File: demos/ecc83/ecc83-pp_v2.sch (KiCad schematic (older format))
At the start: 11 parts, among them P1 IN, P2 OUT, P3 POWER, P4 CONN_2, U1 ECC83

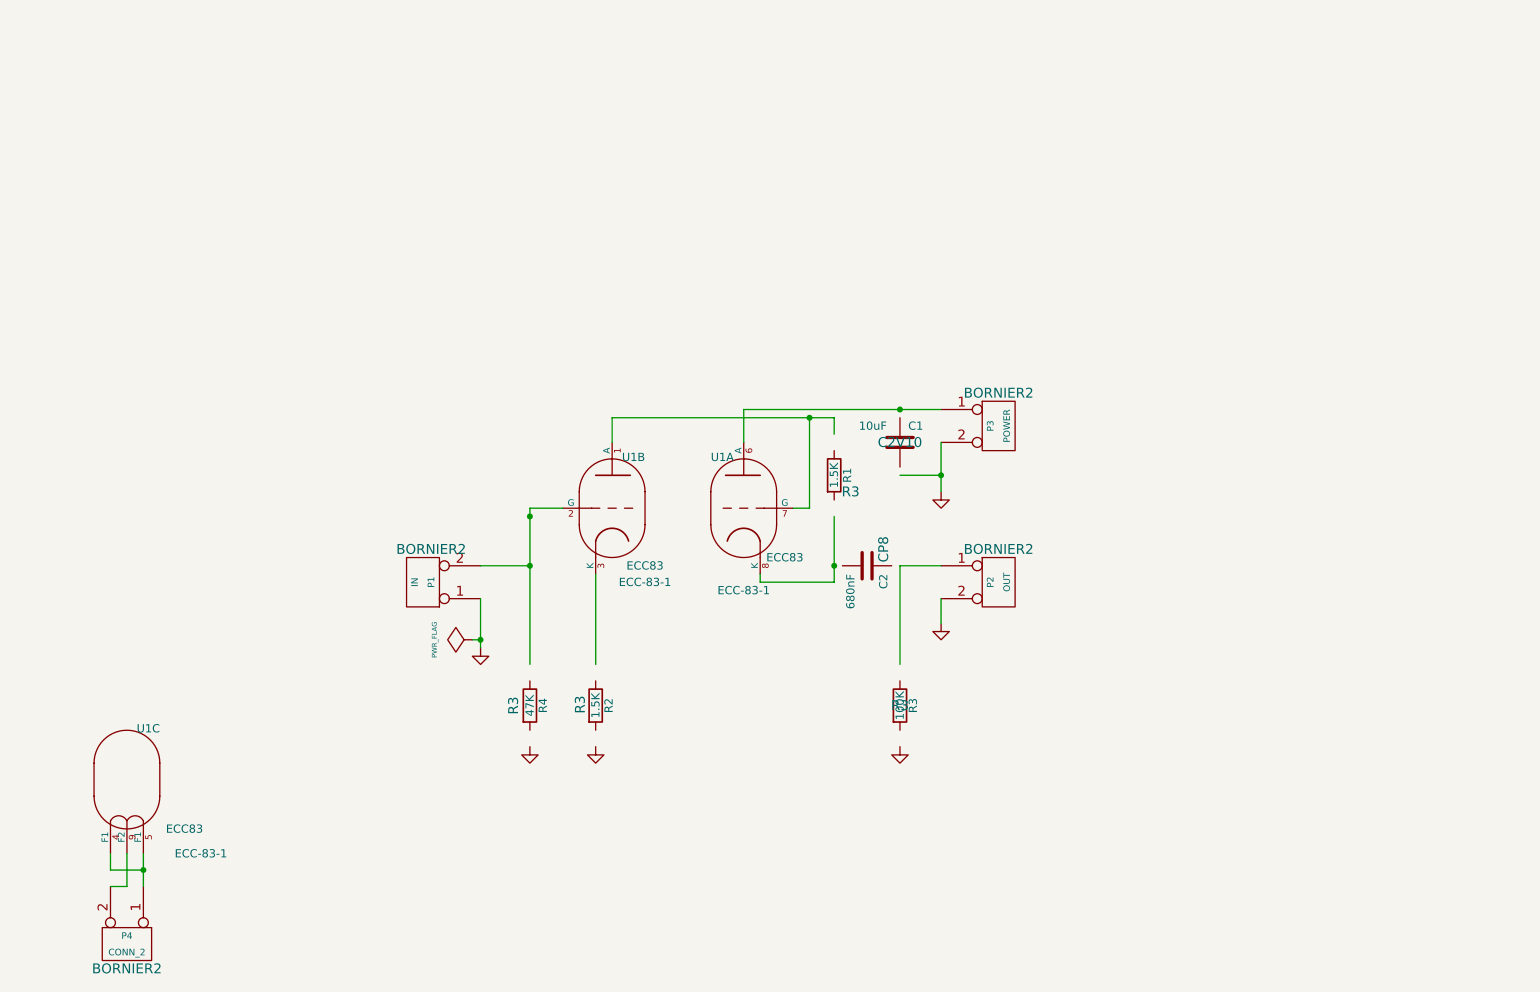
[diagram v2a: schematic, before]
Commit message: Update ecc83 demo. default KISYS3DMOD definition on Linux: add /usr/local/kicad/share/kicad/module/package3d test to find a suitable value.
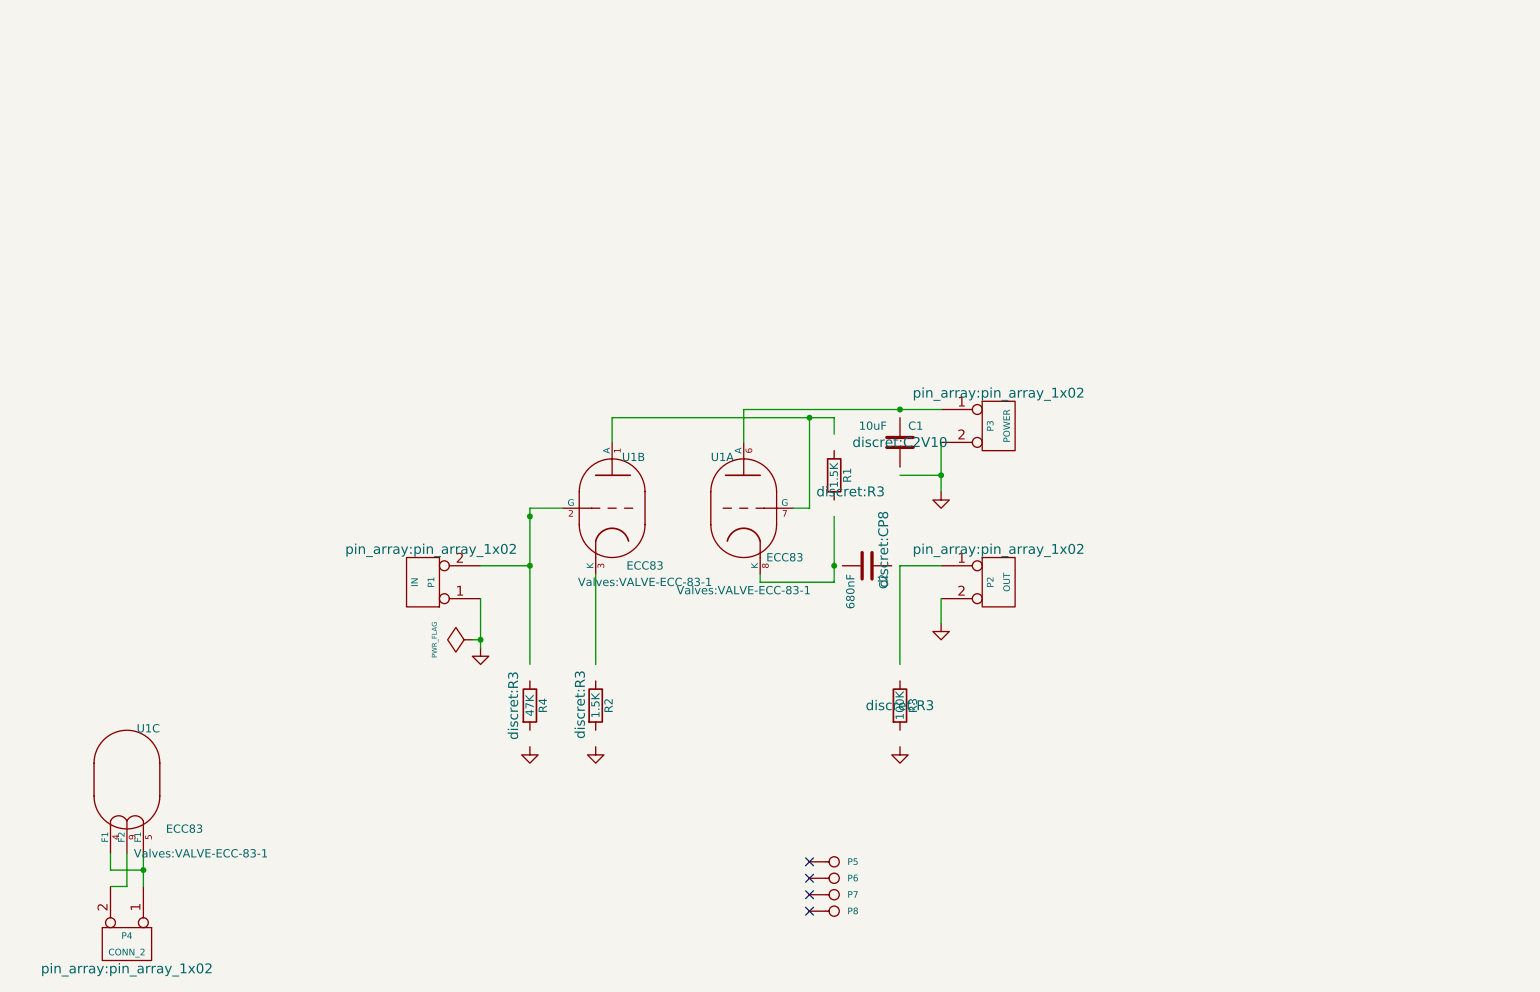
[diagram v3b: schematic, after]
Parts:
- added P5, P6, P7, P8: CONN_1, connect:1pin, symbol CONN_1
- C1: footprint C2V10 -> discret:C2V10
- C2: footprint CP8 -> discret:CP8
- P1, P2, P3, P4: footprint BORNIER2 -> pin_array:pin_array_1x02
- R1, R2, R3, R4: footprint R3 -> discret:R3
- U1: footprint ECC-83-1 -> Valves:VALVE-ECC-83-1
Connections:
- no-connect marks 0 -> 4
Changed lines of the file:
@@
 LIBS:contrib
 LIBS:ecc83-pp_v2-cache
-EELAYER 24 0
+EELAYER 25 0
 EELAYER END
 $Descr A4 11693 8268
@@
 F 0 "U1" H 2130 6410 50  0000 C CNN
 F 1 "ECC83" H 2350 5800 50  0000 C CNN
-F 2 "ECC-83-1" H 2450 5650 50  0000 C CNN
+F 2 "Valves:VALVE-ECC-83-1" H 2450 5650 50  0000 C CNN
 F 3 "" H 2000 6100 60  0001 C CNN
 	3    2000 6100
@@
 F 0 "U1" H 5080 4760 50  0000 C CNN
 F 1 "ECC83" H 5150 4100 50  0000 C CNN
-F 2 "ECC-83-1" H 5150 4000 50  0000 C CNN
+F 2 "Valves:VALVE-ECC-83-1" H 5150 4000 50  0000 C CNN
 F 3 "" H 4950 4450 60  0001 C CNN
 	2    4950 4450
@@
 F 0 "U1" H 5880 4760 50  0000 C CNN
 F 1 "ECC83" H 5500 4150 50  0000 C CNN
-F 2 "ECC-83-1" H 5750 3950 50  0000 C CNN
+F 2 "Valves:VALVE-ECC-83-1" H 5750 3950 50  0000 C CNN
 F 3 "" H 5750 4450 60  0001 C CNN
 	1    5750 4450
@@
 F 0 "P4" V 1950 7100 40  0000 C CNN
 F 1 "CONN_2" V 2050 7100 40  0000 C CNN
-F 2 "BORNIER2" V 2150 7100 60  0000 C CNN
+F 2 "pin_array:pin_array_1x02" V 2150 7100 60  0000 C CNN
 F 3 "" H 2000 7100 60  0001 C CNN
 	1    2000 7100
@@
 F 0 "C1" H 6750 4150 50  0000 L CNN
 F 1 "10uF" H 6450 4150 50  0000 L CNN
-F 2 "C2V10" H 6700 4050 60  0000 C CNN
+F 2 "discret:C2V10" H 6700 4050 60  0000 C CNN
 F 3 "" H 6700 4050 60  0001 C CNN
 	1    6700 4050
@@
 F 0 "P3" V 7250 3950 40  0000 C CNN
 F 1 "POWER" V 7350 3950 40  0000 C CNN
-F 2 "BORNIER2" H 7300 4150 60  0000 C CNN
+F 2 "pin_array:pin_array_1x02" H 7300 4150 60  0000 C CNN
 F 3 "" H 7300 3950 60  0001 C CNN
 	1    7300 3950
@@
 F 0 "P2" V 7250 4900 40  0000 C CNN
 F 1 "OUT" V 7350 4900 40  0000 C CNN
-F 2 "BORNIER2" H 7300 5100 60  0000 C CNN
+F 2 "pin_array:pin_array_1x02" H 7300 5100 60  0000 C CNN
 F 3 "" H 7300 4900 60  0001 C CNN
 	1    7300 4900
@@
 F 0 "P1" V 3750 4900 40  0000 C CNN
 F 1 "IN" V 3850 4900 40  0000 C CNN
-F 2 "BORNIER2" H 3750 4700 60  0000 C CNN
+F 2 "pin_array:pin_array_1x02" H 3750 4700 60  0000 C CNN
 F 3 "" H 3800 4900 60  0001 C CNN
 	1    3800 4900
@@
 F 0 "C2" H 6550 4900 50  0000 L CNN
 F 1 "680nF" H 6550 4700 50  0000 L CNN
-F 2 "CP8" H 6400 4900 60  0000 C CNN
+F 2 "discret:CP8" H 6400 4900 60  0000 C CNN
 F 3 "" H 6500 4800 60  0001 C CNN
 	1    6500 4800
@@
 F 0 "R3" V 6780 5650 50  0000 C CNN
 F 1 "100K" V 6700 5650 50  0000 C CNN
-F 2 "R3" H 6700 5650 60  0000 C CNN
+F 2 "discret:R3" H 6700 5650 60  0000 C CNN
 F 3 "" H 6700 5650 60  0001 C CNN
 	1    6700 5650
@@
 F 0 "R4" V 4530 5650 50  0000 C CNN
 F 1 "47K" V 4450 5650 50  0000 C CNN
-F 2 "R3" V 4350 5650 60  0000 C CNN
+F 2 "discret:R3" V 4350 5650 60  0000 C CNN
 F 3 "" H 4450 5650 60  0001 C CNN
 	1    4450 5650
@@
 F 0 "R2" V 4930 5650 50  0000 C CNN
 F 1 "1.5K" V 4850 5650 50  0000 C CNN
-F 2 "R3" V 4756 5656 60  0000 C CNN
+F 2 "discret:R3" V 4756 5656 60  0000 C CNN
 F 3 "" H 4850 5650 60  0001 C CNN
 	1    4850 5650
@@
 F 0 "R1" V 6380 4250 50  0000 C CNN
 F 1 "1.5K" V 6300 4250 50  0000 C CNN
-F 2 "R3" H 6400 4150 60  0000 C CNN
+F 2 "discret:R3" H 6400 4150 60  0000 C CNN
 F 3 "" H 6300 4250 60  0001 C CNN
 	1    6300 4250
 	1    0    0    -1
 $EndComp
+$Comp
+L CONN_1 P5
+U 1 1 54A5830A
+P 6300 6600
+F 0 "P5" H 6380 6600 40  0000 L CNN
+F 1 "CONN_1" H 6300 6655 30  0001 C CNN
+F 2 "connect:1pin" H 6300 6600 60  0001 C CNN
+F 3 "" H 6300 6600 60  0000 C CNN
+	1    6300 6600
+	1    0    0    -1
+$EndComp
+$Comp
+L CONN_1 P6
+U 1 1 54A58363
+P 6300 6700
+F 0 "P6" H 6380 6700 40  0000 L CNN
+F 1 "CONN_1" H 6300 6755 30  0001 C CNN
+F 2 "connect:1pin" H 6300 6700 60  0001 C CNN
+F 3 "" H 6300 6700 60  0000 C CNN
+	1    6300 6700
+	1    0    0    -1
+$EndComp
+$Comp
+L CONN_1 P7
+U 1 1 54A5837A
+P 6300 6800
+F 0 "P7" H 6380 6800 40  0000 L CNN
+F 1 "CONN_1" H 6300 6855 30  0001 C CNN
+F 2 "connect:1pin" H 6300 6800 60  0001 C CNN
+F 3 "" H 6300 6800 60  0000 C CNN
+	1    6300 6800
+	1    0    0    -1
+$EndComp
+$Comp
+L CONN_1 P8
+U 1 1 54A58391
+P 6300 6900
+F 0 "P8" H 6380 6900 40  0000 L CNN
+F 1 "CONN_1" H 6300 6955 30  0001 C CNN
+F 2 "connect:1pin" H 6300 6900 60  0001 C CNN
+F 3 "" H 6300 6900 60  0000 C CNN
+	1    6300 6900
+	1    0    0    -1
+$EndComp
+NoConn ~ 6150 6600
+NoConn ~ 6150 6700
+NoConn ~ 6150 6800
+NoConn ~ 6150 6900
 $EndSCHEMATC

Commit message: Fix compat with swig 3.03
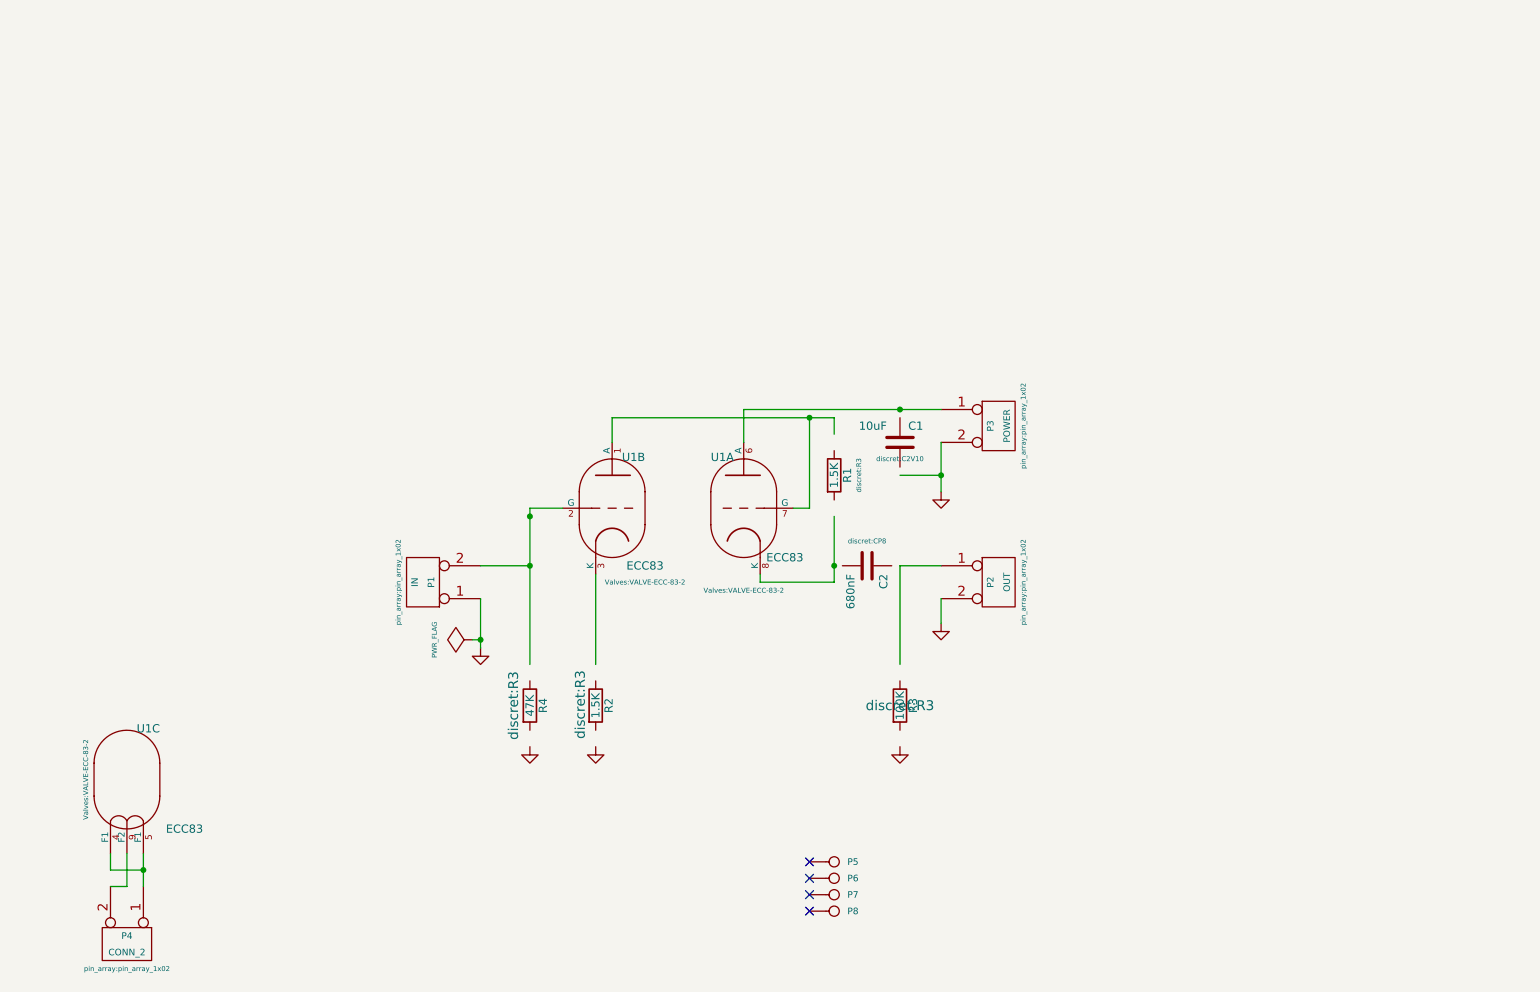
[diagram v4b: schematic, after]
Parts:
- U1: footprint Valves:VALVE-ECC-83-1 -> Valves:VALVE-ECC-83-2
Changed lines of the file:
@@
 LIBS:linear
 LIBS:regul
-LIBS:74xx
-LIBS:cmos4000
-LIBS:adc-dac
-LIBS:memory
-LIBS:xilinx
-LIBS:special
-LIBS:microcontrollers
-LIBS:microchip
-LIBS:analog_switches
-LIBS:motorola
-LIBS:intel
-LIBS:audio
-LIBS:interface
-LIBS:digital-audio
-LIBS:philips
-LIBS:display
-LIBS:cypress
-LIBS:siliconi
-LIBS:contrib
 LIBS:ecc83-pp_v2-cache
 EELAYER 25 0
@@
 F 0 "U1" H 2130 6410 50  0000 C CNN
 F 1 "ECC83" H 2350 5800 50  0000 C CNN
-F 2 "Valves:VALVE-ECC-83-1" H 2450 5650 50  0000 C CNN
+F 2 "Valves:VALVE-ECC-83-2" V 1750 6100 30  0000 C CNN
 F 3 "" H 2000 6100 60  0001 C CNN
 	3    2000 6100
@@
 F 0 "U1" H 5080 4760 50  0000 C CNN
 F 1 "ECC83" H 5150 4100 50  0000 C CNN
-F 2 "Valves:VALVE-ECC-83-1" H 5150 4000 50  0000 C CNN
+F 2 "Valves:VALVE-ECC-83-2" H 5150 4000 30  0000 C CNN
 F 3 "" H 4950 4450 60  0001 C CNN
 	2    4950 4450
@@
 F 0 "U1" H 5880 4760 50  0000 C CNN
 F 1 "ECC83" H 5500 4150 50  0000 C CNN
-F 2 "Valves:VALVE-ECC-83-1" H 5750 3950 50  0000 C CNN
+F 2 "Valves:VALVE-ECC-83-2" H 5750 3950 30  0000 C CNN
 F 3 "" H 5750 4450 60  0001 C CNN
 	1    5750 4450
@@
 F 0 "P4" V 1950 7100 40  0000 C CNN
 F 1 "CONN_2" V 2050 7100 40  0000 C CNN
-F 2 "pin_array:pin_array_1x02" V 2150 7100 60  0000 C CNN
+F 2 "pin_array:pin_array_1x02" V 2150 7100 30  0000 C CNN
 F 3 "" H 2000 7100 60  0001 C CNN
 	1    2000 7100
@@
 F 0 "C1" H 6750 4150 50  0000 L CNN
 F 1 "10uF" H 6450 4150 50  0000 L CNN
-F 2 "discret:C2V10" H 6700 4050 60  0000 C CNN
+F 2 "discret:C2V10" H 6700 3950 30  0000 C CNN
 F 3 "" H 6700 4050 60  0001 C CNN
 	1    6700 4050
@@
 F 0 "P3" V 7250 3950 40  0000 C CNN
 F 1 "POWER" V 7350 3950 40  0000 C CNN
-F 2 "pin_array:pin_array_1x02" H 7300 4150 60  0000 C CNN
+F 2 "pin_array:pin_array_1x02" V 7450 3950 30  0000 C CNN
 F 3 "" H 7300 3950 60  0001 C CNN
 	1    7300 3950
@@
 F 0 "P2" V 7250 4900 40  0000 C CNN
 F 1 "OUT" V 7350 4900 40  0000 C CNN
-F 2 "pin_array:pin_array_1x02" H 7300 5100 60  0000 C CNN
+F 2 "pin_array:pin_array_1x02" V 7450 4900 30  0000 C CNN
 F 3 "" H 7300 4900 60  0001 C CNN
 	1    7300 4900
@@
 F 0 "P1" V 3750 4900 40  0000 C CNN
 F 1 "IN" V 3850 4900 40  0000 C CNN
-F 2 "pin_array:pin_array_1x02" H 3750 4700 60  0000 C CNN
+F 2 "pin_array:pin_array_1x02" V 3950 4900 30  0000 C CNN
 F 3 "" H 3800 4900 60  0001 C CNN
 	1    3800 4900
@@
 F 0 "C2" H 6550 4900 50  0000 L CNN
 F 1 "680nF" H 6550 4700 50  0000 L CNN
-F 2 "discret:CP8" H 6400 4900 60  0000 C CNN
+F 2 "discret:CP8" V 6350 4800 30  0000 C CNN
 F 3 "" H 6500 4800 60  0001 C CNN
 	1    6500 4800
@@
 F 0 "R1" V 6380 4250 50  0000 C CNN
 F 1 "1.5K" V 6300 4250 50  0000 C CNN
-F 2 "discret:R3" H 6400 4150 60  0000 C CNN
+F 2 "discret:R3" V 6450 4250 30  0000 C CNN
 F 3 "" H 6300 4250 60  0001 C CNN
 	1    6300 4250

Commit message: demos/ schematic tidying
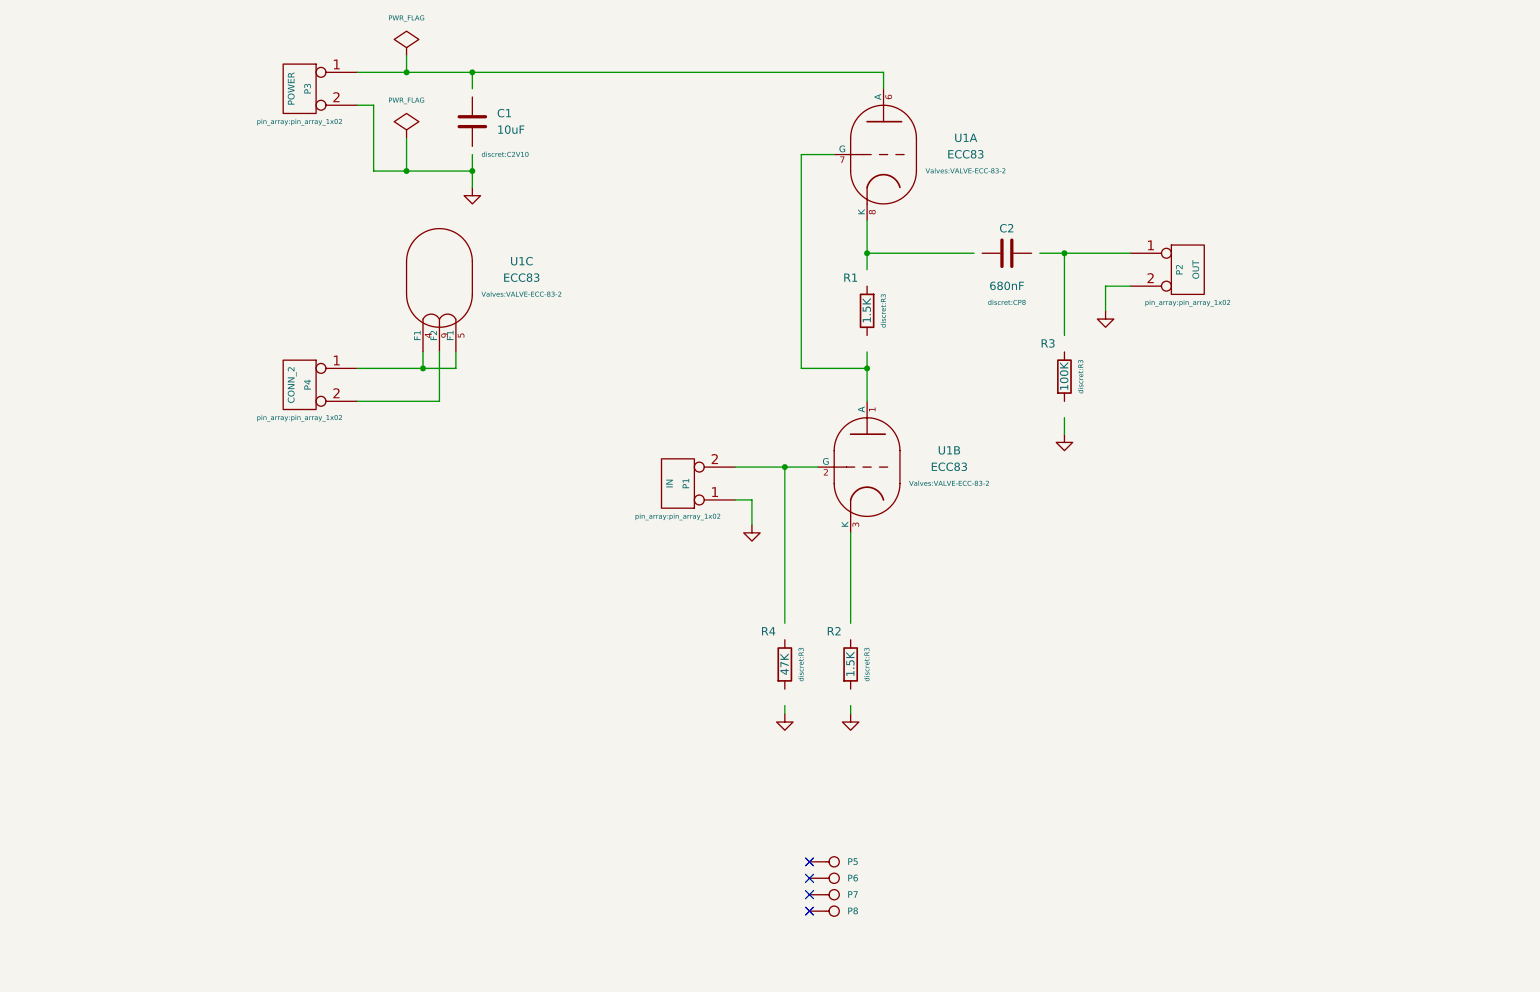
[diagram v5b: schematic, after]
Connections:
- wire segments 26 -> 41
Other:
- moved on the sheet: C1, C2, P1, P2, P3, P4, R1, R2, R3, R4, U1A, U1B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
